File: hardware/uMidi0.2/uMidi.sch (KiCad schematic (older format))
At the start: 20 parts, among them CON1 USB-MINI-B, IC1 ATXMEGA128A4U-M, P1 PDI, U1 74LS14

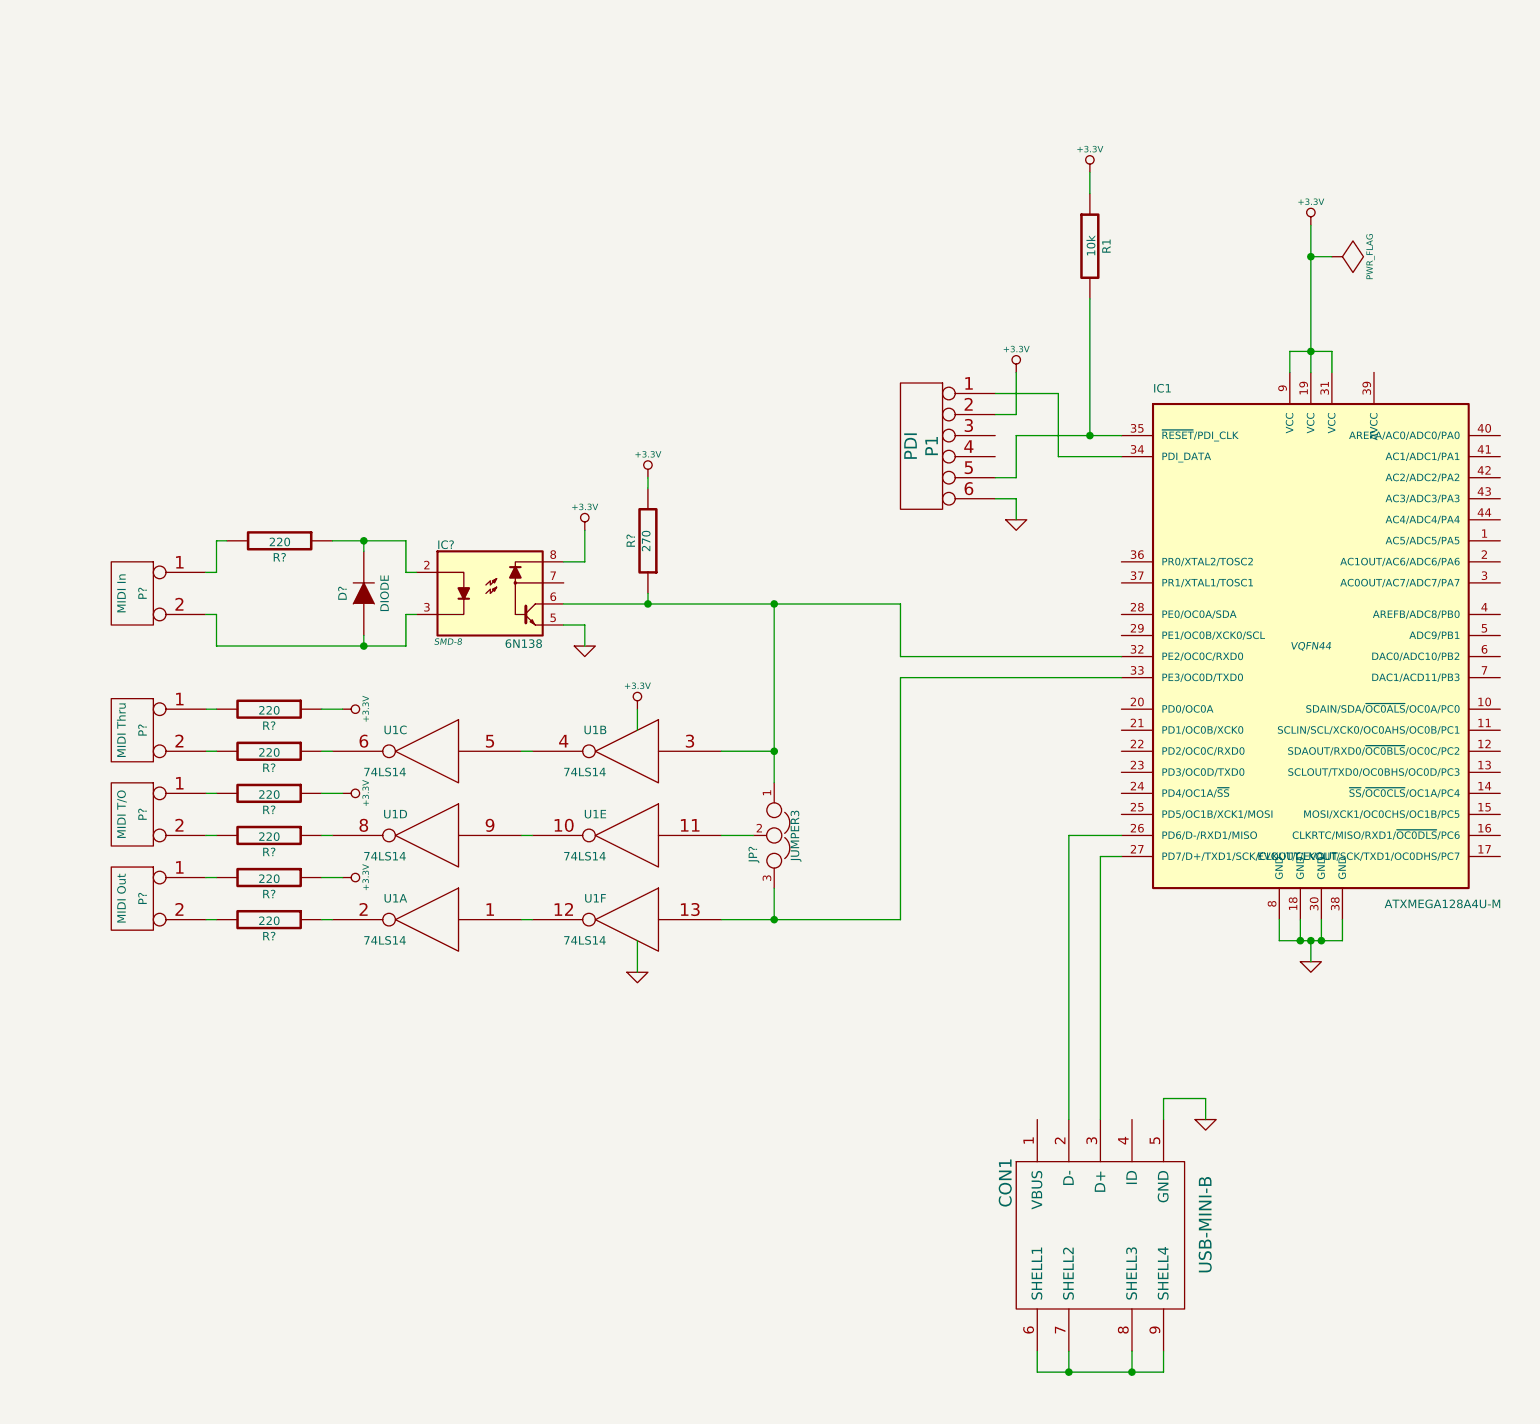
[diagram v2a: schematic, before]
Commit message: Separate midi circuit; Use global labels
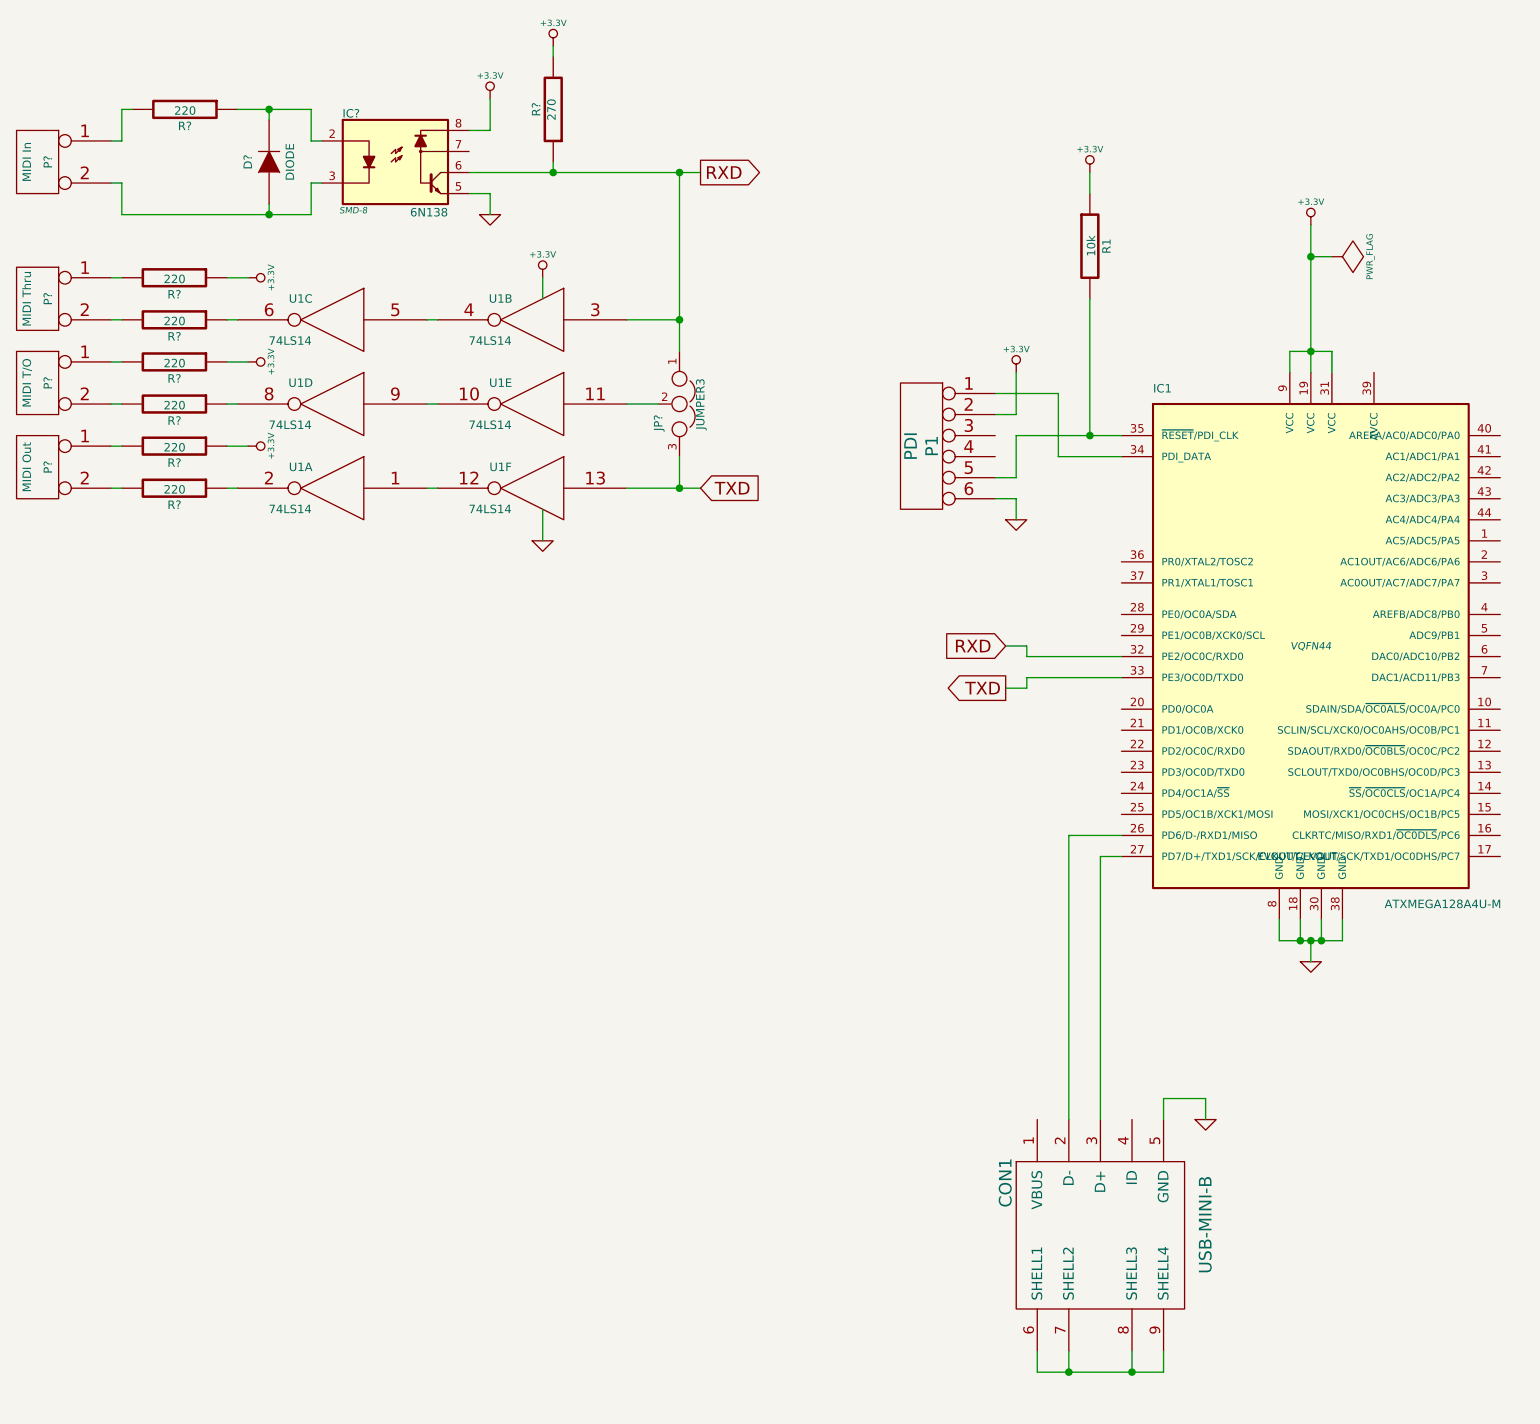
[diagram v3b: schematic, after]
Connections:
- net RXD: now reaches IC1.32 (PE2/OC0C/RXD0), IC?.6, JP?.1, R?.1, U1.3
- net TXD: now reaches IC1.33 (PE3/OC0D/TXD0), JP?.3, U1.13
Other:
- moved on the sheet: D?, IC?, JP?, P?, R?, U1A, U1B, U1C, U1D, U1E, U1F
